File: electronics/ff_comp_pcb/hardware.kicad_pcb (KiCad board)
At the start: 4 copper layers, 50 x 34 mm, 80 parts, among them J1 Micro_SD_Card_Det_Hirose_DM3AT, U1 AS4C512M16D3L-12BIN, U2 A33, Y1 24Mhz, Y2 32.768khz

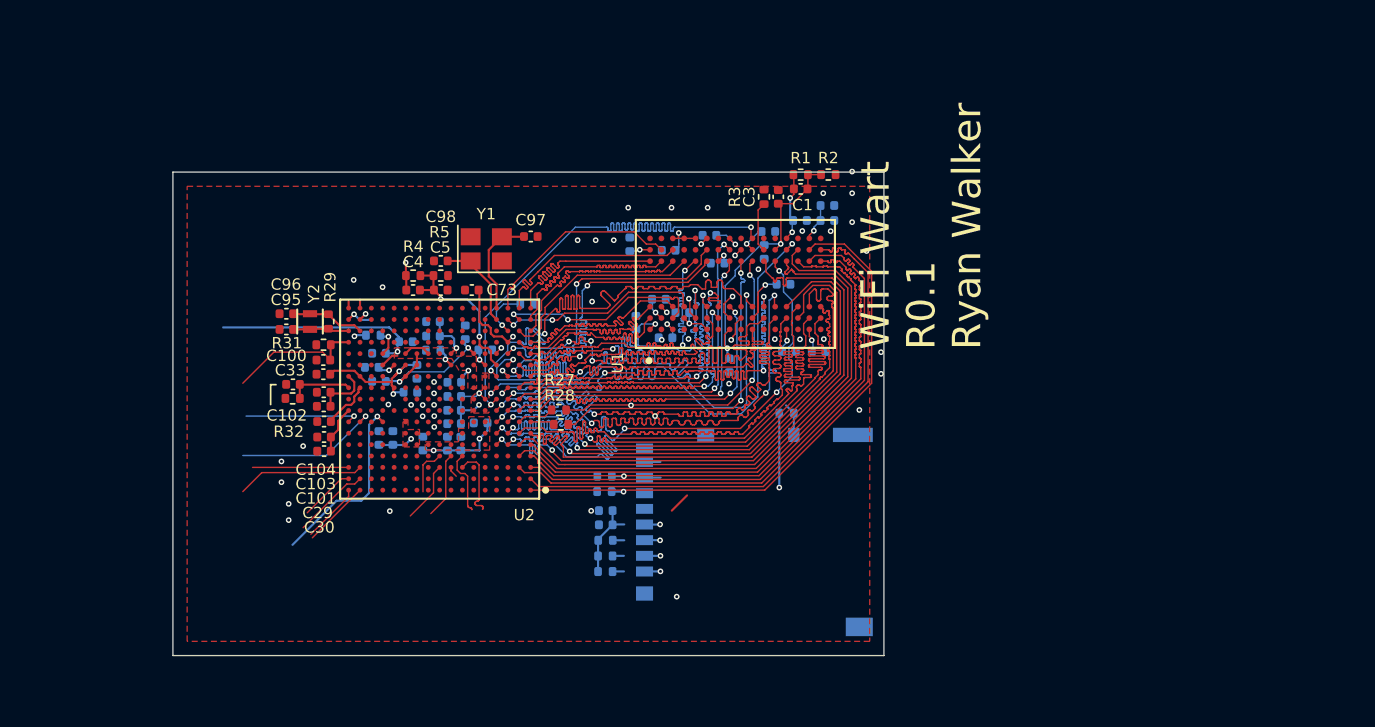
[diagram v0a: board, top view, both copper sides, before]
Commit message: Added the model for the usb, added a USB mux
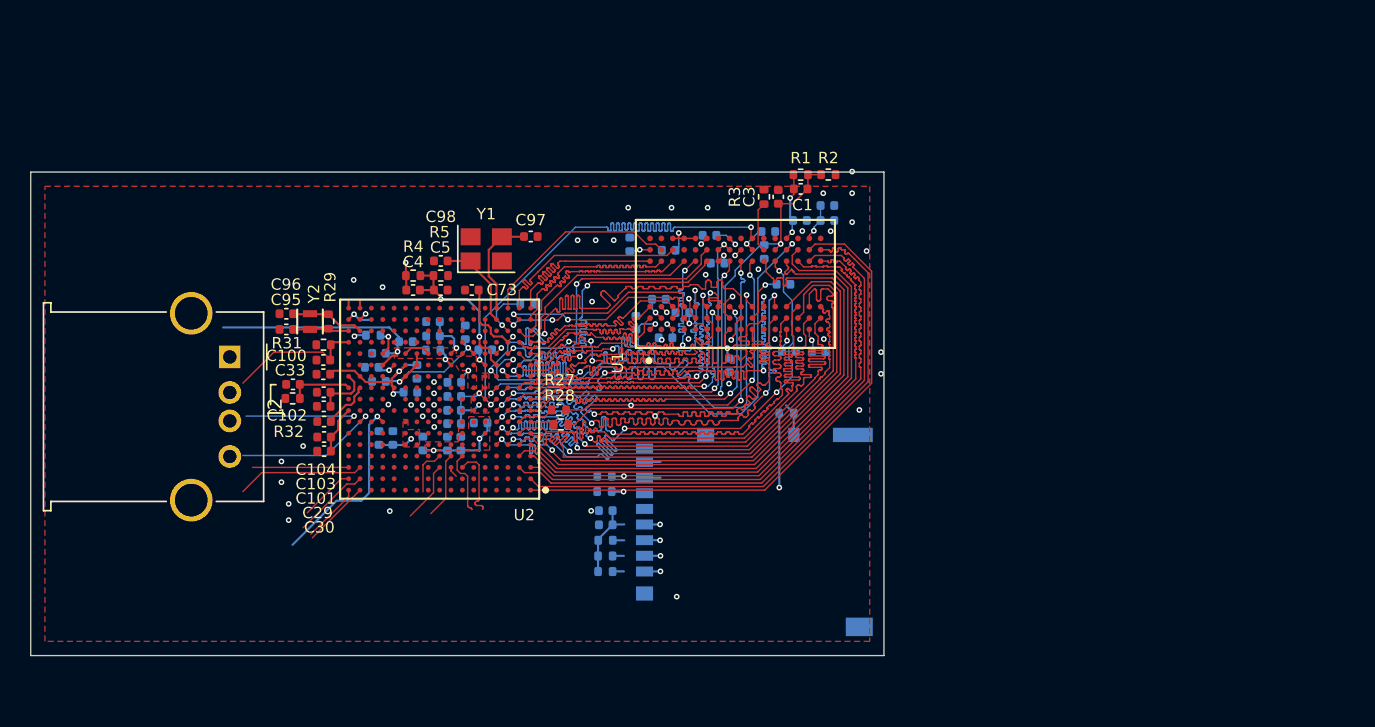
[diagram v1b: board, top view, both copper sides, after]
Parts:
- added J2: USB_A, Connector_USB:USB_A_Molex_67643_Horizontal, F.Cu at (100.0, 106.0)
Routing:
- net +3V3: track 29.1 -> 27.6 mm
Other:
- board size 50 x 34 mm -> 60 x 34 mm
- board text removed: "WiFi Wart R0.1 Ryan Walker"

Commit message: Added the realtek wifi modules
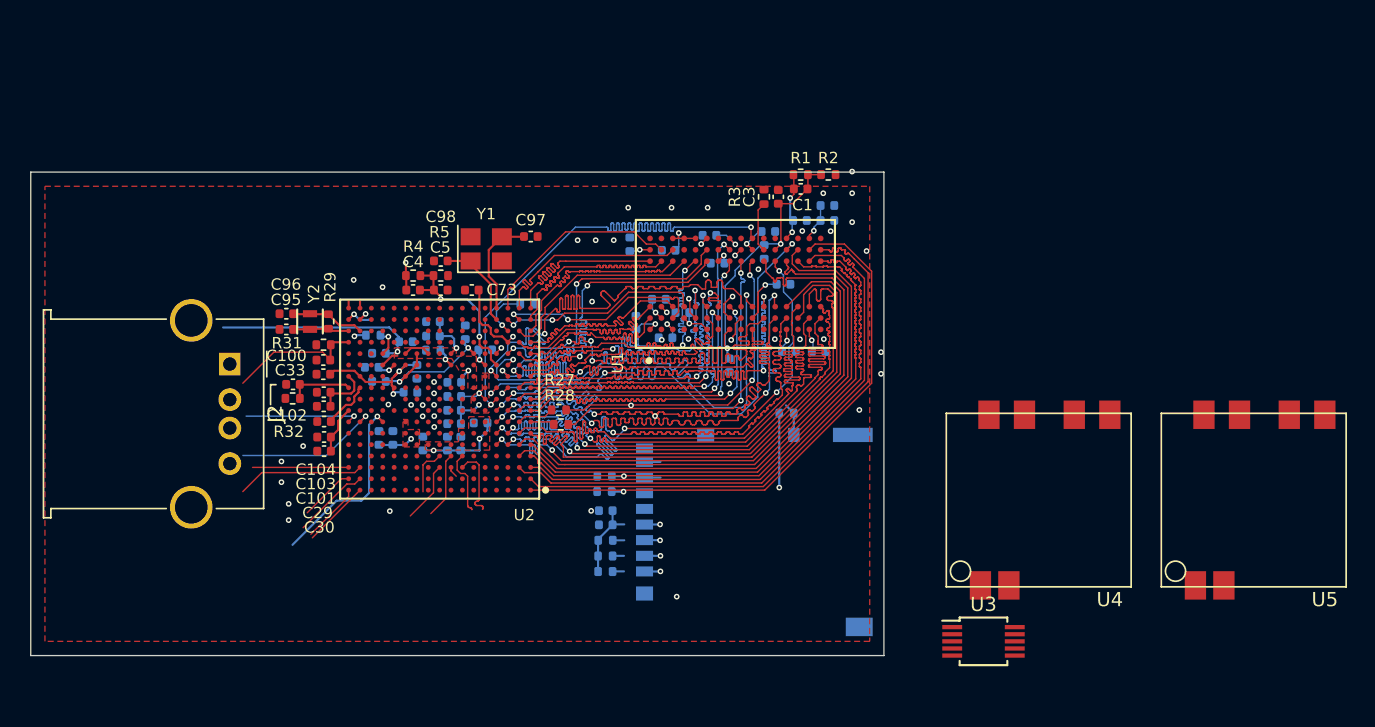
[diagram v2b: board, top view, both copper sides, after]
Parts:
- added U3: FSUSB42MUX, Package_SO:MSOP-10_3x3mm_P0.5mm, F.Cu at (153.0, 126.0)
- added U4: RTL8188CUS, realtek:RTL8188CUS, F.Cu at (156.9, 116.1)
- added U5: RTL8188CUS, realtek:RTL8188CUS, F.Cu at (172.0, 116.1)
- moved J2 0.50 mm to (100.0, 106.5)
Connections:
- J2 pad 1: (no net) -> Net-(J2-Pad1)
- J2 pad 2: (no net) -> Net-(J2-Pad2)
- J2 pad 3: (no net) -> Net-(J2-Pad3)
- J2 pad 4: (no net) -> Net-(J2-Pad4)
- U1 pad J1: (no net) -> Net-(U1-PadJ1)
- U1 pad J9: (no net) -> Net-(U1-PadJ9)
- U1 pad L1: (no net) -> Net-(U1-PadL1)
- U1 pad L9: (no net) -> Net-(U1-PadL9)
- U2 pad A10: (no net) -> Net-(U2-PadA10)
- U2 pad A11: (no net) -> Net-(U2-PadA11)
- U2 pad A12: (no net) -> Net-(U2-PadA12)
- U2 pad A13: (no net) -> Net-(U2-PadA13)
- U2 pad A14: (no net) -> Net-(U2-PadA14)
- U2 pad A15: (no net) -> Net-(U2-PadA15)
- U2 pad A16: (no net) -> /gpio/PG8
- U2 pad A17: (no net) -> /gpio/PG6
- U2 pad A2: (no net) -> Net-(U2-PadA2)
- U2 pad A3: (no net) -> Net-(U2-PadA3)
- U2 pad A4: (no net) -> Net-(U2-PadA4)
- U2 pad A5: (no net) -> Net-(U2-PadA5)
- U2 pad A6: (no net) -> Net-(U2-PadA6)
- U2 pad A7: (no net) -> Net-(U2-PadA7)
- U2 pad A8: (no net) -> Net-(U2-PadA8)
- U2 pad A9: (no net) -> Net-(U2-PadA9)
- U2 pad B10: (no net) -> Net-(U2-PadB10)
- U2 pad B11: (no net) -> Net-(U2-PadB11)
- U2 pad B13: (no net) -> Net-(U2-PadB13)
- U2 pad B14: (no net) -> Net-(U2-PadB14)
- U2 pad B15: (no net) -> Net-(U2-PadB15)
- U2 pad B16: (no net) -> /gpio/PG9
- U2 pad B17: (no net) -> /gpio/PG7
- U2 pad B2: (no net) -> Net-(U2-PadB2)
- U2 pad B3: (no net) -> Net-(U2-PadB3)
- U2 pad B4: (no net) -> Net-(U2-PadB4)
- U2 pad B5: (no net) -> Net-(U2-PadB5)
- U2 pad B6: (no net) -> Net-(U2-PadB6)
- U2 pad B7: (no net) -> Net-(U2-PadB7)
- U2 pad B8: (no net) -> Net-(U2-PadB8)
- U2 pad B9: (no net) -> Net-(U2-PadB9)
- U2 pad C10: (no net) -> Net-(U2-PadC10)
- U2 pad C11: (no net) -> Net-(U2-PadC11)
- U2 pad C12: (no net) -> Net-(U2-PadC12)
- U2 pad C13: (no net) -> Net-(U2-PadC13)
- U2 pad C14: (no net) -> Net-(U2-PadC14)
- U2 pad C15: (no net) -> Net-(U2-PadC15)
- U2 pad C16: (no net) -> /gpio/PG11
- U2 pad C17: (no net) -> /gpio/PG10
- U2 pad C3: (no net) -> Net-(U2-PadC3)
- U2 pad C4: (no net) -> Net-(U2-PadC4)
- U2 pad C5: (no net) -> Net-(U2-PadC5)
- U2 pad C6: (no net) -> Net-(U2-PadC6)
- U2 pad D10: (no net) -> Net-(U2-PadD10)
- U2 pad D11: (no net) -> Net-(U2-PadD11)
- U2 pad D12: (no net) -> Net-(U2-PadD12)
- U2 pad D13: (no net) -> Net-(U2-PadD13)
- U2 pad D14: (no net) -> Net-(U2-PadD14)
- U2 pad D15: (no net) -> Net-(U2-PadD15)
- U2 pad D16: (no net) -> Net-(U2-PadD16)
- U2 pad D17: (no net) -> Net-(U2-PadD17)
- U2 pad D3: (no net) -> Net-(U2-PadD3)
- U2 pad D4: (no net) -> Net-(U2-PadD4)
- U2 pad D5: (no net) -> Net-(U2-PadD5)
- U2 pad D6: (no net) -> Net-(U2-PadD6)
- U2 pad E14: (no net) -> Net-(U2-PadE14)
- U2 pad E15: (no net) -> Net-(U2-PadE15)
- U2 pad E16: (no net) -> Net-(U2-PadE16)
- U2 pad E17: (no net) -> Net-(U2-PadE17)
- U2 pad F14: (no net) -> Net-(U2-PadF14)
- U2 pad F15: (no net) -> Net-(U2-PadF15)
- U2 pad F16: (no net) -> Net-(U2-PadF16)
- U2 pad F17: (no net) -> Net-(U2-PadF17)
- U2 pad G15: (no net) -> Net-(U2-PadG15)
- U2 pad G16: (no net) -> /gpio/UART0_RX
- U2 pad G17: (no net) -> /gpio/UART0_TX
- U2 pad H14: (no net) -> Net-(U2-PadH14)
- U2 pad H15: (no net) -> Net-(U2-PadH15)
- U2 pad H16: (no net) -> Net-(U2-PadH16)
- U2 pad J14: (no net) -> Net-(U2-PadJ14)
- U2 pad J15: (no net) -> Net-(U2-PadJ15)
- U2 pad J16: (no net) -> Net-(U2-PadJ16)
- U2 pad J17: (no net) -> Net-(U2-PadJ17)
- U2 pad K14: (no net) -> Net-(U2-PadK14)
- U2 pad K15: (no net) -> Net-(U2-PadK15)
- U2 pad L14: (no net) -> Net-(U2-PadL14)
- U2 pad L15: (no net) -> Net-(U2-PadL15)
- U2 pad L7: (no net) -> Net-(U2-PadL7)
- U2 pad M15: (no net) -> Net-(U2-PadM15)
- U2 pad M16: (no net) -> Net-(U2-PadM16)
- U2 pad M17: (no net) -> Net-(U2-PadM17)
- U2 pad N15: (no net) -> Net-(U2-PadN15)
- U2 pad N16: (no net) -> Net-(U2-PadN16)
- U2 pad N17: (no net) -> Net-(U2-PadN17)
- U2 pad N5: (no net) -> Net-(U2-PadN5)
- U2 pad N7: (no net) -> Net-(U2-PadN7)
- U2 pad P10: (no net) -> Net-(U2-PadP10)
- U2 pad P11: (no net) -> Net-(U2-PadP11)
- U2 pad P12: (no net) -> Net-(U2-PadP12)
- U2 pad P13: (no net) -> Net-(U2-PadP13)
- U2 pad P14: (no net) -> Net-(U2-PadP14)
- U2 pad P15: (no net) -> Net-(U2-PadP15)
- U2 pad P16: (no net) -> Net-(U2-PadP16)
- U2 pad P4: (no net) -> Net-(U2-PadP4)
- U2 pad P5: (no net) -> Net-(U2-PadP5)
- U2 pad P6: (no net) -> Net-(U2-PadP6)
- U2 pad P7: (no net) -> Net-(U2-PadP7)
- U2 pad P8: (no net) -> Net-(U2-PadP8)
- U2 pad P9: (no net) -> Net-(U2-PadP9)
- U2 pad R10: (no net) -> Net-(U2-PadR10)
- U2 pad R11: (no net) -> Net-(U2-PadR11)
- U2 pad R12: (no net) -> Net-(U2-PadR12)
- U2 pad R13: (no net) -> Net-(U2-PadR13)
- U2 pad R14: (no net) -> Net-(U2-PadR14)
- U2 pad R15: (no net) -> Net-(U2-PadR15)
- U2 pad R4: (no net) -> Net-(U2-PadR4)
- U2 pad R5: (no net) -> Net-(U2-PadR5)
- U2 pad R6: (no net) -> Net-(U2-PadR6)
- U2 pad R7: (no net) -> Net-(U2-PadR7)
- U2 pad R8: (no net) -> Net-(U2-PadR8)
- U2 pad R9: (no net) -> Net-(U2-PadR9)
- U2 pad T10: (no net) -> Net-(U2-PadT10)
- U2 pad T11: (no net) -> Net-(U2-PadT11)
- U2 pad T12: (no net) -> Net-(U2-PadT12)
- U2 pad T13: (no net) -> Net-(U2-PadT13)
- U2 pad T14: (no net) -> Net-(U2-PadT14)
- U2 pad T15: (no net) -> Net-(U2-PadT15)
- U2 pad T16: (no net) -> Net-(U2-PadT16)
- U2 pad T17: (no net) -> Net-(U2-PadT17)
- U2 pad T5: (no net) -> Net-(U2-PadT5)
- U2 pad T6: (no net) -> Net-(U2-PadT6)
- U2 pad T7: (no net) -> Net-(U2-PadT7)
- U2 pad T8: (no net) -> Net-(U2-PadT8)
- U2 pad T9: (no net) -> Net-(U2-PadT9)
- U2 pad U10: (no net) -> Net-(U2-PadU10)
- U2 pad U11: (no net) -> Net-(U2-PadU11)
- U2 pad U12: (no net) -> Net-(U2-PadU12)
- U2 pad U13: (no net) -> Net-(U2-PadU13)
- U2 pad U14: (no net) -> Net-(U2-PadU14)
- U2 pad U15: (no net) -> Net-(U2-PadU15)
- U2 pad U16: (no net) -> Net-(U2-PadU16)
- U2 pad U17: (no net) -> Net-(U2-PadU17)
- U2 pad U5: (no net) -> Net-(U2-PadU5)
- U2 pad U6: (no net) -> Net-(U2-PadU6)
- U2 pad U7: (no net) -> Net-(U2-PadU7)
- U2 pad U8: (no net) -> Net-(U2-PadU8)
- U2 pad U9: (no net) -> Net-(U2-PadU9)
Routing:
- net (no net): track 56.0 -> 0.00 mm, vias 4 -> 0
- net /gpio/UART0_RX: track 0.00 -> 10.3 mm, vias 0 -> 1
- net /gpio/PG11: track 0.00 -> 8.95 mm
- net /gpio/UART0_TX: track 0.00 -> 8.16 mm, vias 0 -> 1
- net /gpio/PG10: track 0.00 -> 6.76 mm
- net /gpio/PG9: track 0.00 -> 5.43 mm
- net /gpio/PG8: track 0.00 -> 4.74 mm
- net /gpio/PG6: track 0.00 -> 4.20 mm
- net /gpio/PG7: track 0.00 -> 3.90 mm
- net Net-(U2-PadT17): track 0.00 -> 1.74 mm, vias 0 -> 1
- net Net-(U2-PadU16): track 0.00 -> 0.62 mm
- net Net-(U2-PadU17): track 0.00 -> 0.56 mm
- net Net-(U2-PadT16): track 0.00 -> 0.56 mm, vias 0 -> 1

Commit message: Fit the radios on the board.
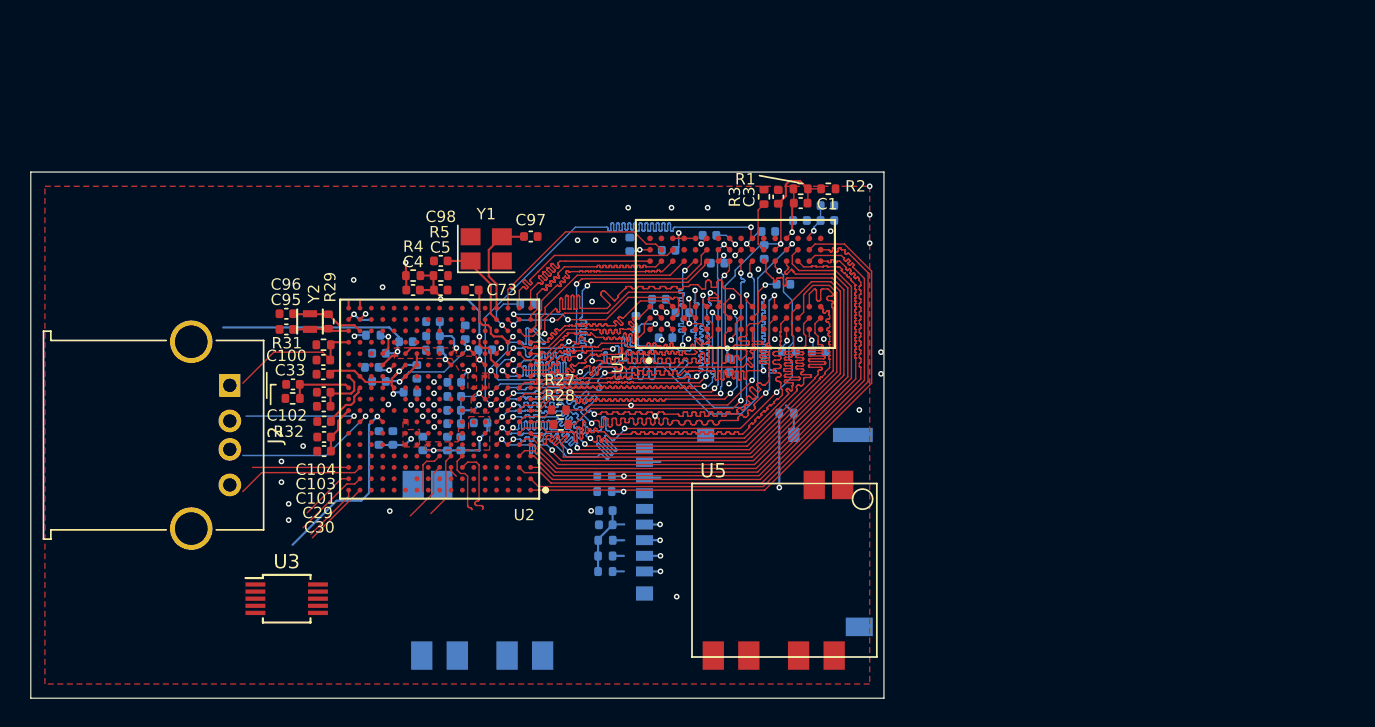
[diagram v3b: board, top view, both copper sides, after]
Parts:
- U4: moved to B.Cu
- moved U3 49.1 mm to (104.0, 123.0)
- moved U4 40.2 mm to (117.0, 121.0)
- moved U5 33.4 mm to (139.0, 121.0), turned to 180 degrees
- moved J2 1.50 mm to (100.0, 108.0)
- moved C1 1.00 mm to (140.1, 95.2)
- moved R1 1.00 mm to (140.1, 94.2)
- moved R2 1.00 mm to (142.1, 94.2)
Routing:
- net Net-(C1-Pad2): track 20.1 -> 21.0 mm
- net +1V35: vias 19 -> 18
- net GND: vias 48 -> 46
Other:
- board size 60 x 34 mm -> 60 x 37 mm
